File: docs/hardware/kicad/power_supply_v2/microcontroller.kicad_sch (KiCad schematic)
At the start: 1 part, among them U10 NUCLEO-G474RE

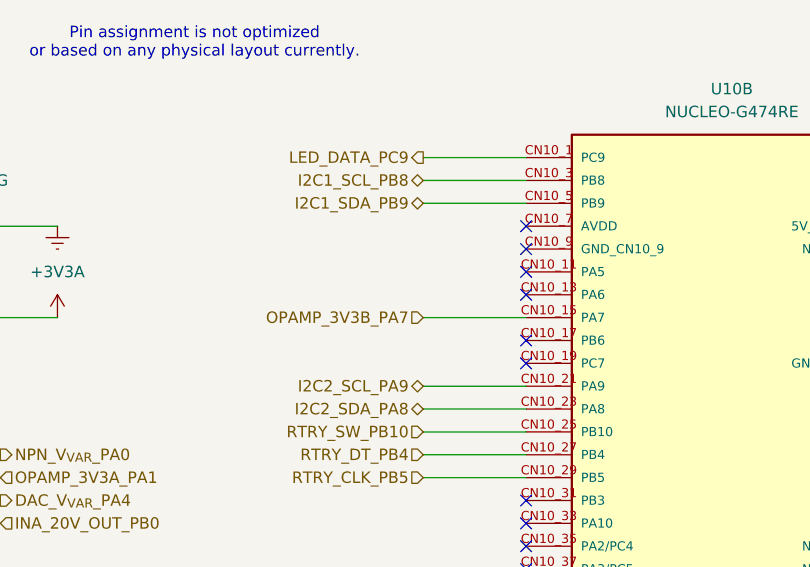
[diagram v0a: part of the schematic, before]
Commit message: updated schematic for LC filters and added voltage injection to other bucks
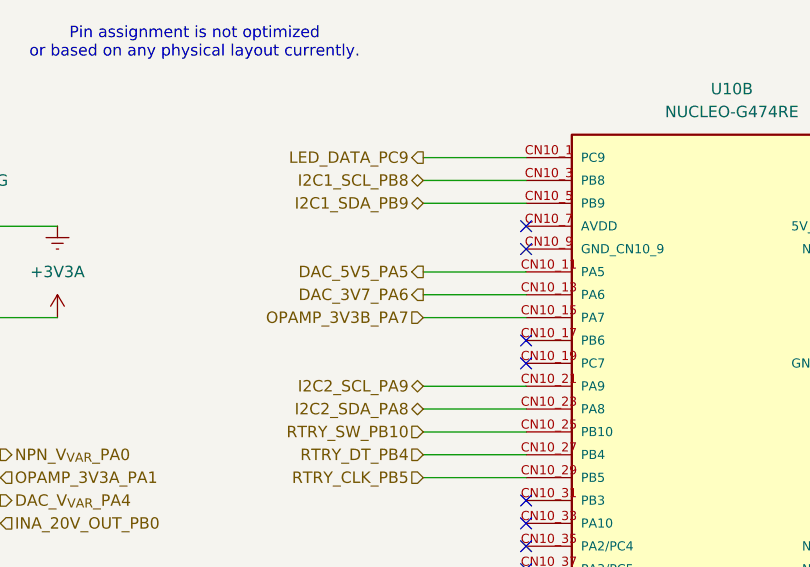
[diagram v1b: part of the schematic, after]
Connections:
- net DAC_5V5_PA5: now reaches U10.CN10_11 (PA5)
- net DAC_3V7_PA6: now reaches U10.CN10_13 (PA6)
- no-connect marks 39 -> 37
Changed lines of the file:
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@@
-	)
-	(no_connect
-		(at 186.69 81.28)
 	)
 	(no_connect
@@
 	)
 	(no_connect
-		(at 186.69 78.74)
-	)
-	(no_connect
 		(at 186.69 88.9)
 	)
@@
 	(wire
 		(pts
+			(xy 175.26 78.74) (xy 186.69 78.74)
+		)
+		(stroke
+			(width 0)
+			(type default)
+		)
+	)
+	(wire
+		(pts
 			(xy 60.96 109.22) (xy 72.39 109.22)
 		)
@@
 	(wire
 		(pts
+			(xy 175.26 81.28) (xy 186.69 81.28)
+		)
+		(stroke
+			(width 0)
+			(type default)
+		)
+	)
+	(wire
+		(pts
 			(xy 232.41 66.04) (xy 242.57 66.04)
 		)
@@
 			(width 0)
 			(type default)
+		)
+	)
+	(hierarchical_label "DAC_5V5_PA5"
+		(shape output)
+		(at 175.26 78.74 180)
+		(effects
+			(font
+				(size 1.27 1.27)
+			)
+			(justify right)
 		)
 	)
@@
 		(effects
 			(font
+				(size 1.27 1.27)
+			)
+			(justify right)
+		)
+	)
+	(hierarchical_label "DAC_3V7_PA6"
+		(shape output)
+		(at 175.26 81.28 180)
+		(effects
+			(font

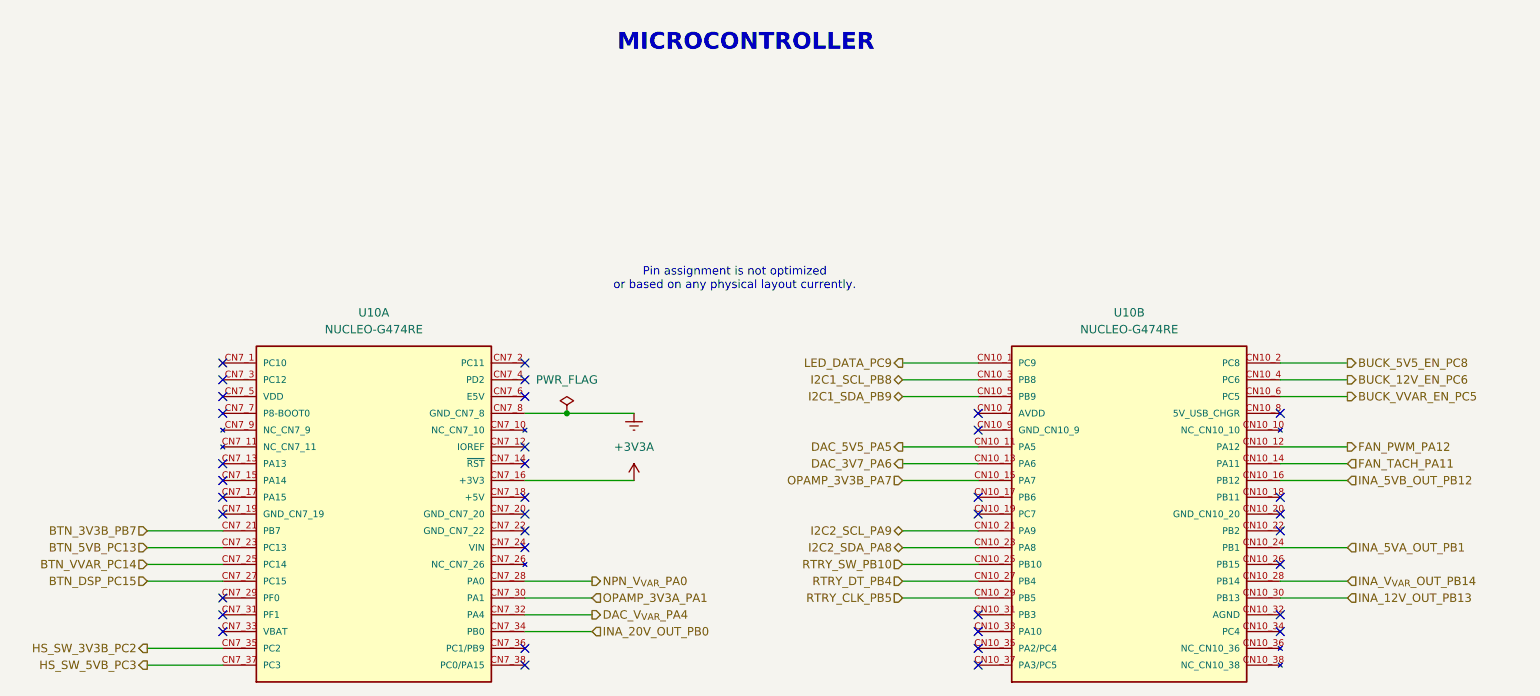
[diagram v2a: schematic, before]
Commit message: remove redundant switches for variable rail
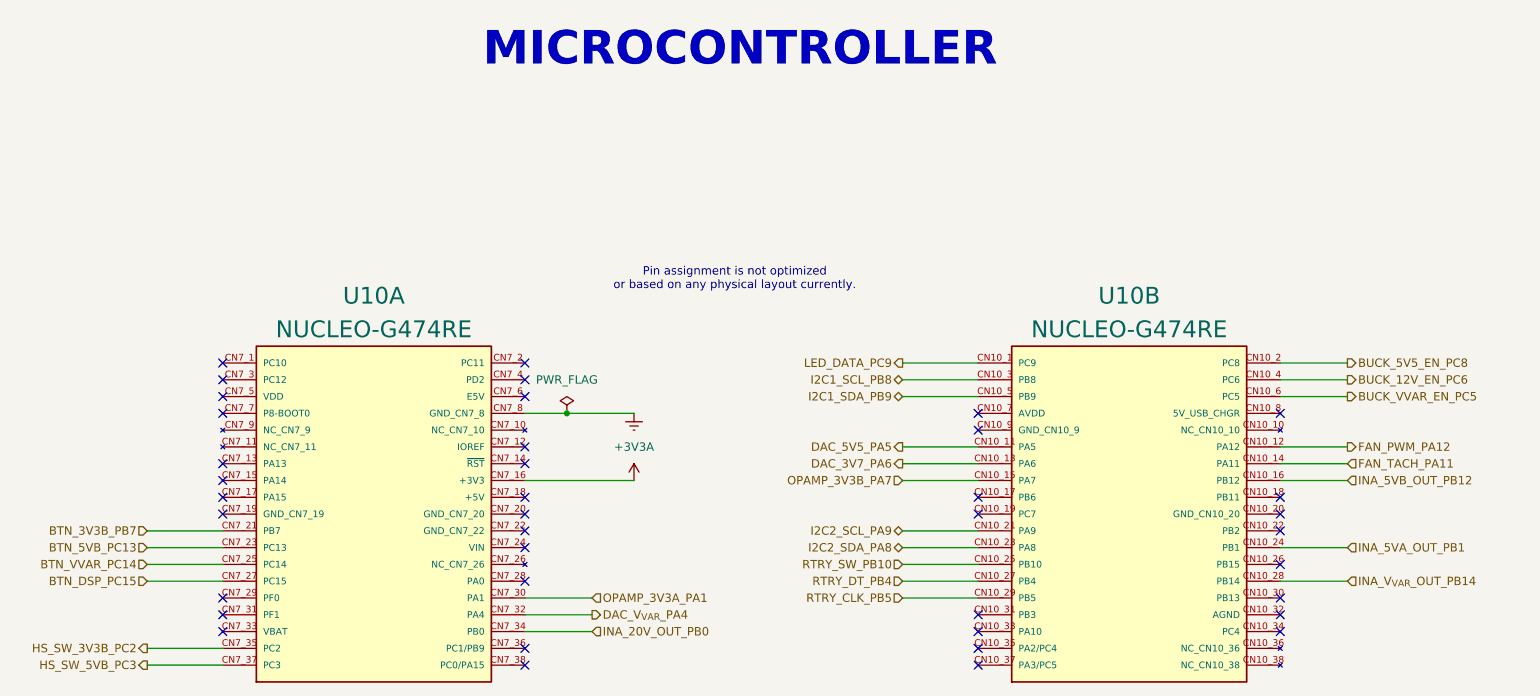
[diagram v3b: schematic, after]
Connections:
- net INA_12V_OUT_PB13: no longer names the net of U10.CN10_30 (PB13)
- net NPN_V_{VAR}_PA0: no longer names the net of U10.CN7_28 (PA0)
- no-connect marks 37 -> 39
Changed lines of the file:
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@@
 	(title_block
 		(title "Digital Variable DC Bench Power Supply")
-		(date "2026-04-30")
-		(rev "A2")
+		(date "2026-05-01")
+		(rev "A3")
 	)
 	(text "MICROCONTROLLER"
 		(exclude_from_sim no)
-		(at 132.08 19.05 0)
-		(effects
-			(font
-				(size 2.54 2.54)
+		(at 111.76 21.59 0)
+		(effects
+			(font
+				(size 5.08 5.08)
 				(thickness 1.016)
 				(bold yes)
@@
 	)
 	(no_connect
+		(at 232.41 101.6)
+	)
+	(no_connect
 		(at 118.11 68.58)
 	)
@@
 	)
 	(no_connect
+		(at 118.11 99.06)
+	)
+	(no_connect
 		(at 118.11 81.28)
 	)
@@
 	(wire
 		(pts
-			(xy 232.41 101.6) (xy 242.57 101.6)
-		)
-		(stroke
-			(width 0)
-			(type default)
-		)
-	)
-	(wire
-		(pts
 			(xy 175.26 101.6) (xy 186.69 101.6)
 		)
@@
 		(pts
 			(xy 118.11 106.68) (xy 128.27 106.68)
-		)
-		(stroke
-			(width 0)
-			(type default)
-		)
-	)
-	(wire
-		(pts
-			(xy 118.11 99.06) (xy 128.27 99.06)
 		)
 		(stroke
@@
 		)
 	)
-	(hierarchical_label "INA_12V_OUT_PB13"
-		(shape input)
-		(at 242.57 101.6 0)
-		(effects
-			(font
-				(size 1.27 1.27)
-			)
-			(justify left)
-		)
-	)
 	(hierarchical_label "DAC_V_{VAR}_PA4"
 		(shape output)
@@
 			)
 			(justify right)
-		)
-	)
-	(hierarchical_label "NPN_V_{VAR}_PA0"
-		(shape output)
-		(at 128.27 99.06 0)
-		(effects
-			(font
-				(size 1.27 1.27)
-			)
-			(justify left)
 		)
 	)
@@
 		(on_board yes)
 		(dnp no)
-		(fields_autoplaced yes)
 		(property "Reference" "U10"
-			(at 95.25 58.42 0)
-			(effects
-				(font
-					(size 1.27 1.27)
+			(at 95.25 55.88 0)
+			(effects
+				(font
+					(size 2.54 2.54)
 				)
 			)
@@
 			(effects
 				(font
-					(size 1.27 1.27)
+					(size 2.54 2.54)
 				)
 			)
@@
 		(on_board yes)
 		(dnp no)
-		(fields_autoplaced yes)
 		(property "Reference" "U10"
-			(at 209.55 58.42 0)
-			(effects
-				(font
-					(size 1.27 1.27)
+			(at 209.55 55.88 0)
+			(effects
+				(font
+					(size 2.54 2.54)
 				)
 			)
@@
 			(effects
 				(font
-					(size 1.27 1.27)
-				)
-			)
+					(size 2.54 2.54)
+				)
+			)

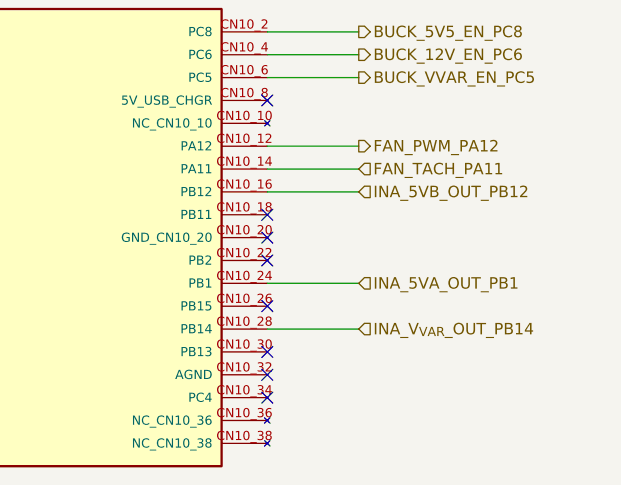
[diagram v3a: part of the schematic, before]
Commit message: update schematic to fix power rail node and update resistors to reflect series to reach target dividers
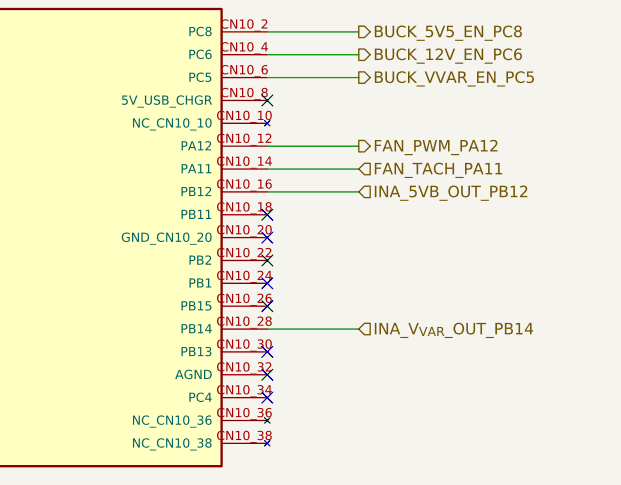
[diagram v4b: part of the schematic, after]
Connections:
- net INA_5VA_OUT_PB1: no longer names the net of U10.CN10_24 (PB1)
- no-connect marks 39 -> 40
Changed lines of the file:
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@@
 	(title_block
 		(title "Digital Variable DC Bench Power Supply")
-		(date "2026-05-01")
-		(rev "A3")
+		(date "2026-05-06")
+		(rev "A4")
 	)
 	(text "MICROCONTROLLER"
@@
 	)
 	(no_connect
+		(at 232.41 93.98)
+	)
+	(no_connect
 		(at 232.41 104.14)
 	)
@@
 		(pts
 			(xy 232.41 68.58) (xy 242.57 68.58)
-		)
-		(stroke
-			(width 0)
-			(type default)
-		)
-	)
-	(wire
-		(pts
-			(xy 232.41 93.98) (xy 242.57 93.98)
 		)
 		(stroke
@@
 		)
 	)
-	(hierarchical_label "INA_5VA_OUT_PB1"
-		(shape input)
-		(at 242.57 93.98 0)
-		(effects
-			(font
-				(size 1.27 1.27)
-			)
-			(justify left)
-		)
-	)
